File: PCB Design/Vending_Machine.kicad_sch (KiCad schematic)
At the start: 0 parts

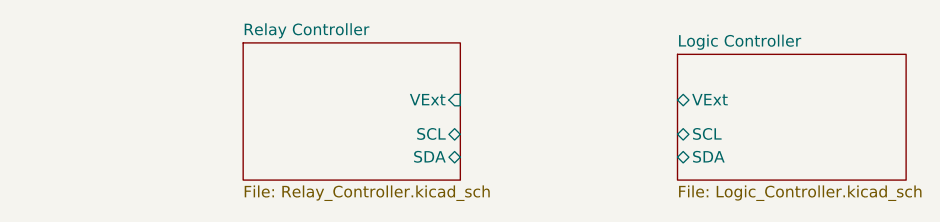
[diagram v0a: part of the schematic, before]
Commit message: Panelize
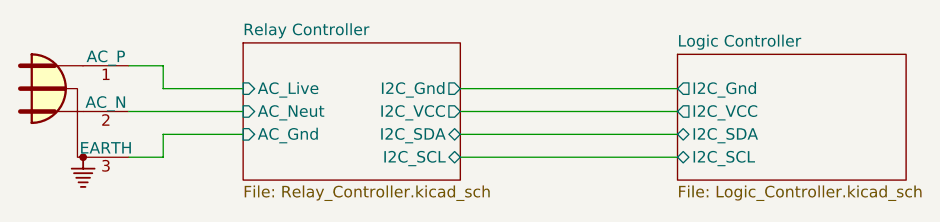
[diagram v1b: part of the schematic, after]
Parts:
- added P01: Main Supply, symbol Connector:Conn_WallPlug_Earth
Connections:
- new net Relay Controller/AC_Gnd: P01.3 (EARTH)
- new net Relay Controller/AC_Live: P01.1 (AC_P)
- new net Relay Controller/AC_Neut: P01.2 (AC_N)
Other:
- sheet Logic Controller ports: added I2C_Gnd, I2C_SCL, I2C_SDA, I2C_VCC; removed SCL, SDA, VExt
- sheet Relay Controller ports: added AC_Gnd, AC_Live, AC_Neut, I2C_Gnd, I2C_SCL, I2C_SDA, I2C_VCC; removed SCL, SDA, VExt
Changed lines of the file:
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@@
 		(comment 1 "Penny Wood")
+	)
+	(wire
+		(pts
+			(xy 97.79 66.04) (xy 121.92 66.04)
+		)
+		(stroke
+			(width 0)
+			(type default)
+		)
+	)
+	(wire
+		(pts
+			(xy 64.77 55.88) (xy 64.77 58.42)
+		)
+		(stroke
+			(width 0)
+			(type default)
+		)
+	)
+	(wire
+		(pts
+			(xy 97.79 60.96) (xy 121.92 60.96)
+		)
+		(stroke
+			(width 0)
+			(type default)
+		)
+	)
+	(wire
+		(pts
+			(xy 97.79 58.42) (xy 121.92 58.42)
+		)
+		(stroke
+			(width 0)
+			(type default)
+		)
+	)
+	(wire
+		(pts
+			(xy 97.79 63.5) (xy 121.92 63.5)
+		)
+		(stroke
+			(width 0)
+			(type default)
+		)
+	)
+	(wire
+		(pts
+			(xy 60.96 66.04) (xy 64.77 66.04)
+		)
+		(stroke
+			(width 0)
+			(type default)
+		)
+	)
+	(wire
+		(pts
+			(xy 60.96 55.88) (xy 64.77 55.88)
+		)
+		(stroke
+			(width 0)
+			(type default)
+		)
+	)
+	(wire
+		(pts
+			(xy 64.77 66.04) (xy 64.77 63.5)
+		)
+		(stroke
+			(width 0)
+			(type default)
+		)
+	)
+	(wire
+		(pts
+			(xy 60.96 60.96) (xy 73.66 60.96)
+		)
+		(stroke
+			(width 0)
+			(type default)
+		)
+	)
+	(wire
+		(pts
+			(xy 64.77 58.42) (xy 73.66 58.42)
+		)
+		(stroke
+			(width 0)
+			(type default)
+		)
+	)
+	(wire
+		(pts
+			(xy 64.77 63.5) (xy 73.66 63.5)
+		)
+		(stroke
+			(width 0)
+			(type default)
+		)
+	)
+	(symbol
+		(lib_id "Connector:Conn_WallPlug_Earth")
+		(at 53.34 58.42 0)
+		(unit 1)
+		(exclude_from_sim no)
+		(in_bom yes)
+		(on_board no)
+		(dnp no)
+		(property "Reference" "P01"
+			(at 52.9463 49.53 0)
+			(effects
+				(font
+					(size 1.27 1.27)
+				)
+				(hide yes)
+			)
+		)
+		(property "Value" "Main Supply"
+			(at 52.9463 52.07 0)
+			(effects
+				(font
+					(size 1.27 1.27)
+				)
+				(hide yes)
+			)
+		)
+		(property "Footprint" ""
+			(at 63.5 58.42 0)
+			(effects
+				(font
+					(size 1.27 1.27)
+				)
+				(hide yes)
+			)
+		)
+		(property "Datasheet" "~"
+			(at 63.5 58.42 0)
+			(effects
+				(font
+					(size 1.27 1.27)
+				)
+				(hide yes)
+			)
+		)
+		(property "Description" "3-pin general wall plug, with Earth wire (110VAC, 220VAC)"
+			(at 53.34 58.42 0)
+			(effects
+				(font
+					(size 1.27 1.27)
+				)
+				(hide yes)
+			)
+		)
+		(pin "1"
+		)
+		(pin "2"
+		)
+		(pin "3"
+		)
+		(instances
+			(project "Vending_Machine"
+				(path "/061ecb1c-afb0-4b5f-8f93-1c1ad8e1529c"
+					(reference "P01")
+					(unit 1)
+				)
+			)
+		)
 	)
 	(sheet
@@
 			)
 		)
-		(pin "VExt" bidirectional
-			(at 121.92 59.69 180)
-			(effects
-				(font
-					(size 1.27 1.27)
-				)
-				(justify left)
-			)
-		)
-		(pin "SCL" bidirectional
+		(pin "I2C_SCL" bidirectional
+			(at 121.92 66.04 180)
+			(effects
+				(font
+					(size 1.27 1.27)
+				)
+				(justify left)
+			)
+		)
+		(pin "I2C_Gnd" output
+			(at 121.92 58.42 180)
+			(effects
+				(font
+					(size 1.27 1.27)
+				)
+				(justify left)
+			)
+		)
+		(pin "I2C_SDA" bidirectional
 			(at 121.92 63.5 180)
 			(effects
@@
 			)
 		)
-		(pin "SDA" bidirectional
-			(at 121.92 66.04 180)
+		(pin "I2C_VCC" output
+			(at 121.92 60.96 180)
 			(effects
 				(font
@@
 			)
 		)
-		(pin "VExt" input
-			(at 97.79 59.69 0)
+		(pin "AC_Gnd" input
+			(at 73.66 63.5 180)
+			(effects
+				(font
+					(size 1.27 1.27)
+				)
+				(justify left)
+			)
+		)
+		(pin "AC_Neut" input
+			(at 73.66 60.96 180)
+			(effects
+				(font
+					(size 1.27 1.27)
+				)
+				(justify left)
+			)
+		)
+		(pin "AC_Live" input
+			(at 73.66 58.42 180)
+			(effects
+				(font
+					(size 1.27 1.27)
+				)
+				(justify left)
+			)
+		)
+		(pin "I2C_VCC" output
+			(at 97.79 60.96 0)
 			(effects
 				(font
@@
 			)
 		)
-		(pin "SCL" bidirectional
+		(pin "I2C_Gnd" output
+			(at 97.79 58.42 0)
+			(effects
+				(font
+					(size 1.27 1.27)
+				)
+				(justify right)
+			)
+		)
+		(pin "I2C_SDA" bidirectional
 			(at 97.79 63.5 0)
 			(effects
@@
 			)
 		)
-		(pin "SDA" bidirectional
+		(pin "I2C_SCL" bidirectional
 			(at 97.79 66.04 0)
 			(effects

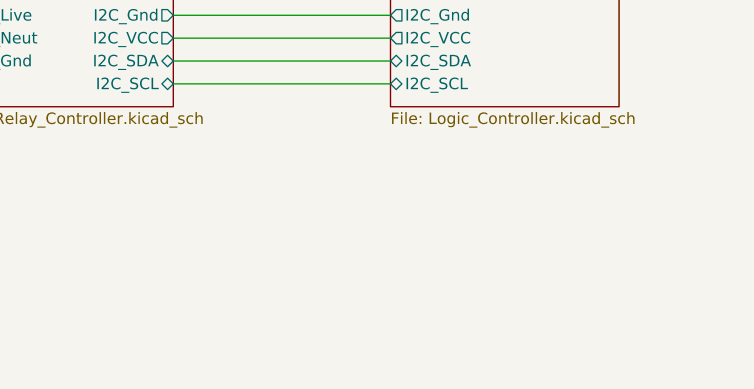
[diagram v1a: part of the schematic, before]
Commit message: Added Multiplexer
Added separate IO Multiplexer breakout
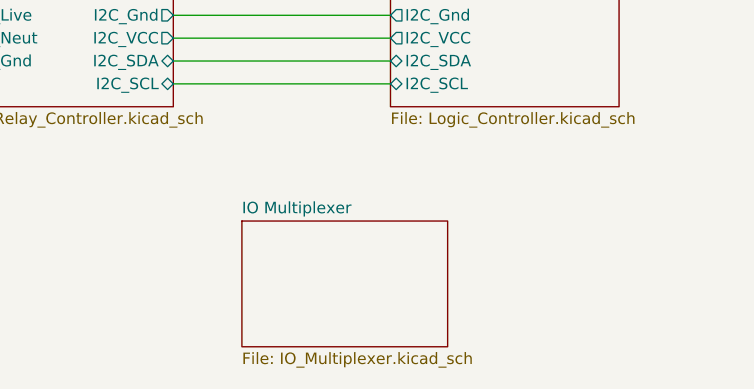
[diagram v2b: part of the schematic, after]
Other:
- added sheet IO Multiplexer (IO_Multiplexer.kicad_sch)
- title: I2C Relay Controler -> Vending Machine
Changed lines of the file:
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@@
 	(paper "A4")
 	(title_block
-		(title "I2C Relay Controler")
+		(title "Vending Machine")
 		(date "2024-03-19")
 		(rev "2")
@@
 				)
 			)
+		)
+	)
+	(sheet
+		(at 105.41 81.28)
+		(size 22.86 13.97)
+		(fields_autoplaced yes)
+		(stroke
+			(width 0.1524)
+			(type solid)
+		)
+		(fill
+			(color 0 0 0 0.0000)
+		)
+		(property "Sheetname" "IO Multiplexer"
+			(at 105.41 80.5684 0)
+			(effects
+				(font
+					(size 1.27 1.27)
+				)
+				(justify left bottom)
+			)
+		)
+		(property "Sheetfile" "IO_Multiplexer.kicad_sch"
+			(at 105.41 95.8346 0)
+			(effects
+				(font
+					(size 1.27 1.27)
+				)
+				(justify left top)
+			)
+		)
+		(instances
+			(project "Vending_Machine"
+				(path "/061ecb1c-afb0-4b5f-8f93-1c1ad8e1529c"
+					(page "4")
+				)
+			)

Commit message: Minor Improvements
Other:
- sheet IO Multiplexer ports: added I2C_Gnd, I2C_SCL, I2C_SDA, I2C_VCC; removed none
- note added: "I2C Bus"

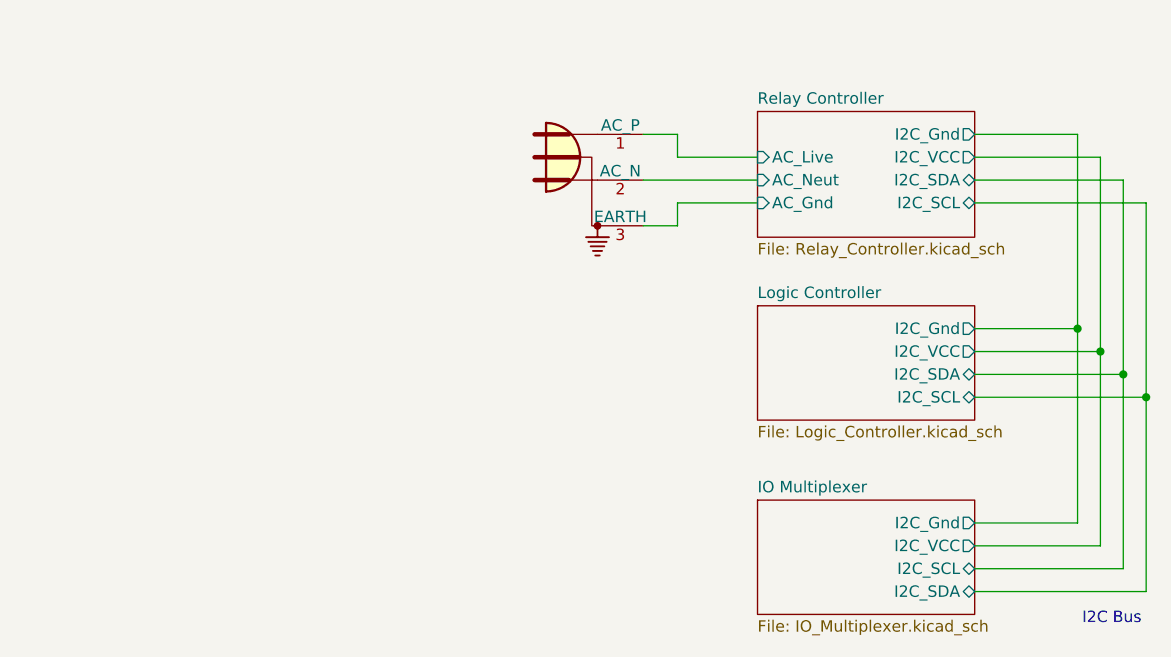
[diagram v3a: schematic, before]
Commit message: Vcc->3v3 Added extra GPIO
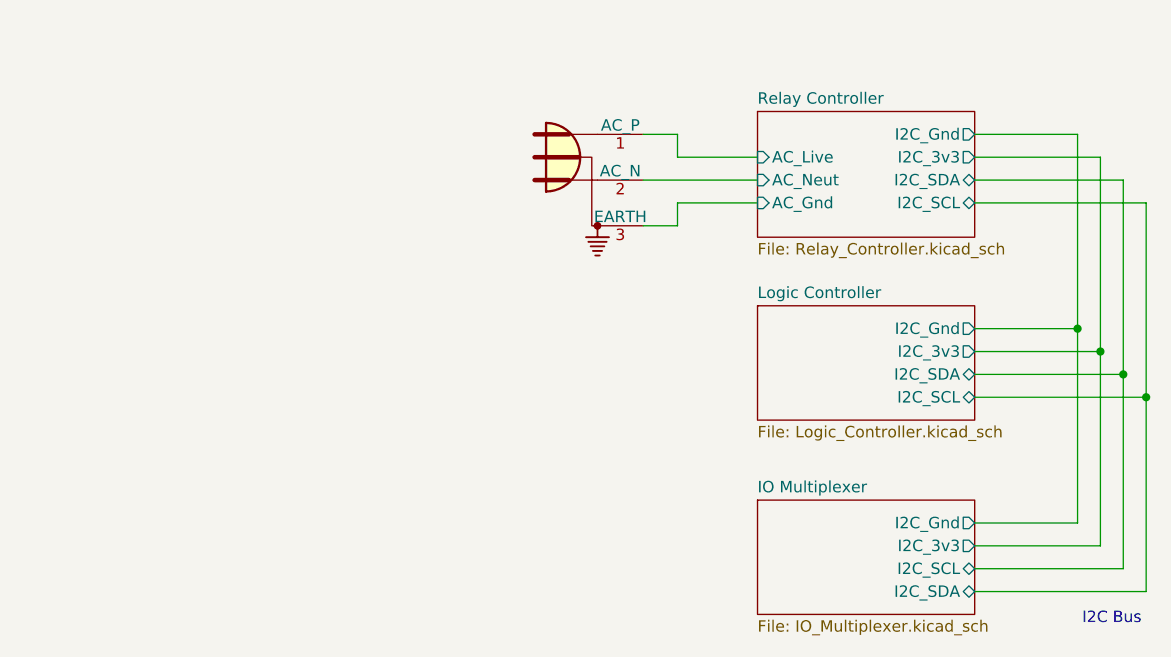
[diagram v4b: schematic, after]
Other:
- sheet IO Multiplexer ports: added I2C_3v3; removed I2C_VCC
- sheet Logic Controller ports: added I2C_3v3; removed I2C_VCC
- sheet Relay Controller ports: added I2C_3v3; removed I2C_VCC
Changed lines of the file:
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@@
 			)
 		)
-		(pin "I2C_VCC" output
+		(pin "I2C_3v3" output
 			(at 154.94 87.63 0)
 			(effects
@@
 			)
 		)
-		(pin "I2C_VCC" output
+		(pin "I2C_3v3" output
 			(at 154.94 109.22 0)
 			(effects
@@
 			)
 		)
-		(pin "I2C_VCC" output
+		(pin "I2C_3v3" output
 			(at 154.94 66.04 0)
 			(effects
